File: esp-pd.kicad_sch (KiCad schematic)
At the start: 83 parts, among them J1 USB C Power, J2 USB C Data, J3 Power Out, J4 ESP PD Board pins, Q1 IRF7416, Q2 MMBT3904, SW1 Boot, SW2 Reset, SW3 Up, SW4 Down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

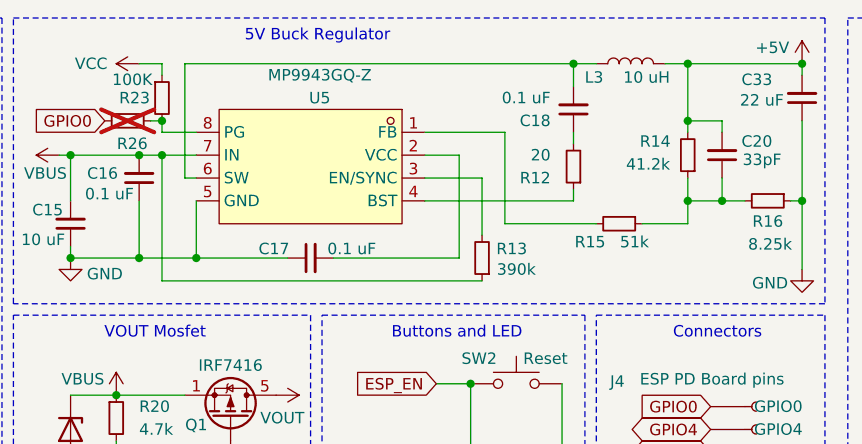
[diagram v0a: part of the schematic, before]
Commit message: added BST diode
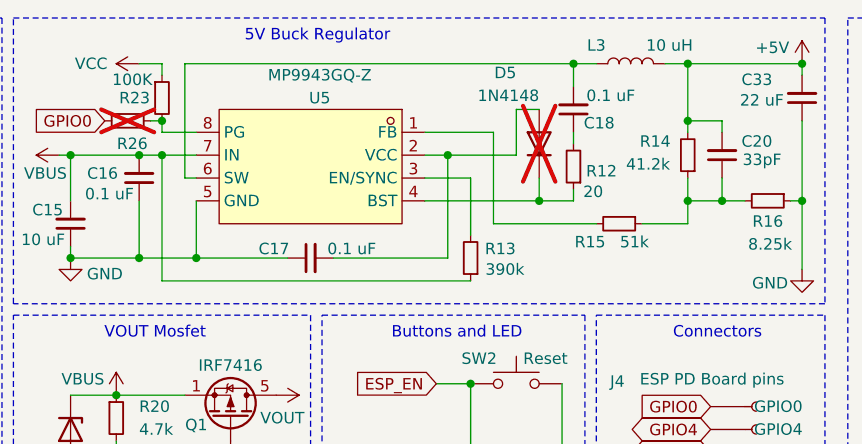
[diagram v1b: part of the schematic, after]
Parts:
- added D5: 1N4148, Diode_SMD:D_SOD-523, symbol Diode:1N4148WT
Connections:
- net at C17.2, U5.2 (VCC): now also D5.2 (A)
- net at R12.1, U5.4 (BST): now also D5.1 (K)
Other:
- moved on the sheet: R13
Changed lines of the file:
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@@
 	)
 	(junction
+		(at 149.86 31.75)
+		(diameter 0)
+		(color 0 0 0 0)
+	)
+	(junction
 		(at 57.15 95.25)
 		(diameter 0)
@@
 	)
 	(junction
+		(at 160.02 36.83)
+		(diameter 0)
+		(color 0 0 0 0)
+	)
+	(junction
 		(at 214.63 58.42)
 		(diameter 0)
@@
 	(wire
 		(pts
-			(xy 118.11 45.72) (xy 153.67 45.72)
+			(xy 118.11 45.72) (xy 152.4 45.72)
 		)
 		(stroke
@@
 	(wire
 		(pts
-			(xy 156.21 29.21) (xy 156.21 39.37)
+			(xy 154.94 29.21) (xy 154.94 39.37)
 		)
 		(stroke
@@
 	(wire
 		(pts
-			(xy 147.32 34.29) (xy 153.67 34.29)
+			(xy 147.32 34.29) (xy 152.4 34.29)
 		)
 		(stroke
@@
 	(wire
 		(pts
-			(xy 147.32 29.21) (xy 156.21 29.21)
+			(xy 147.32 29.21) (xy 154.94 29.21)
+		)
+		(stroke
+			(width 0)
+			(type default)
+		)
+	)
+	(wire
+		(pts
+			(xy 160.02 36.83) (xy 147.32 36.83)
 		)
 		(stroke
@@
 	(wire
 		(pts
-			(xy 151.13 43.18) (xy 151.13 31.75)
+			(xy 149.86 43.18) (xy 149.86 31.75)
 		)
 		(stroke
@@
 	(wire
 		(pts
-			(xy 156.21 39.37) (xy 166.37 39.37)
+			(xy 154.94 39.37) (xy 166.37 39.37)
 		)
 		(stroke
@@
 	(wire
 		(pts
-			(xy 137.16 43.18) (xy 151.13 43.18)
+			(xy 137.16 43.18) (xy 149.86 43.18)
 		)
 		(stroke
@@
 	(wire
 		(pts
-			(xy 151.13 31.75) (xy 147.32 31.75)
+			(xy 149.86 31.75) (xy 147.32 31.75)
 		)
 		(stroke
@@
 	(wire
 		(pts
-			(xy 153.67 34.29) (xy 153.67 40.64)
+			(xy 152.4 34.29) (xy 152.4 40.64)
 		)
 		(stroke
@@
 	(wire
 		(pts
+			(xy 160.02 26.67) (xy 157.48 26.67)
+		)
+		(stroke
+			(width 0)
+			(type default)
+		)
+	)
+	(wire
+		(pts
 			(xy 118.11 88.9) (xy 125.73 88.9)
 		)
@@
 	(wire
 		(pts
-			(xy 163.83 36.83) (xy 147.32 36.83)
+			(xy 163.83 36.83) (xy 160.02 36.83)
+		)
+		(stroke
+			(width 0)
+			(type default)
+		)
+	)
+	(wire
+		(pts
+			(xy 160.02 34.29) (xy 160.02 36.83)
 		)
 		(stroke
@@
 	(wire
 		(pts
+			(xy 157.48 31.75) (xy 149.86 31.75)
+		)
+		(stroke
+			(width 0)
+			(type default)
+		)
+	)
+	(wire
+		(pts
 			(xy 207.01 99.06) (xy 213.36 99.06)
 		)
@@
 	(wire
 		(pts
+			(xy 157.48 26.67) (xy 157.48 31.75)
+		)
+		(stroke
+			(width 0)
+			(type default)
+		)
+	)
+	(wire
+		(pts
 			(xy 121.92 29.21) (xy 118.11 29.21)
 		)
@@
 		(dnp no)
 		(property "Reference" "L3"
-			(at 166.116 23.114 90)
+			(at 166.37 19.558 90)
 			(effects
 				(font
@@
 		)
 		(property "Value" "10 uH"
-			(at 171.958 23.114 90)
+			(at 174.498 19.558 90)
 			(effects
 				(font
@@
 		(on_board yes)
 		(dnp no)
-		(fields_autoplaced yes)
 		(property "Reference" "C18"
-			(at 161.29 27.9338 0)
+			(at 168.402 28.194 0)
 			(effects
 				(font
@@
 		)
 		(property "Value" "0.1 uF"
-			(at 161.29 25.3938 0)
+			(at 170.688 25.146 0)
 			(effects
 				(font
@@
 	)
 	(symbol
+		(lib_id "Diode:1N4148WT")
+		(at 160.02 30.48 90)
+		(unit 1)
+		(exclude_from_sim no)
+		(in_bom yes)
+		(on_board yes)
+		(dnp yes)
+		(property "Reference" "D5"
+			(at 157.48 22.606 90)
+			(effects
+				(font
+					(size 1.27 1.27)
+				)
+				(justify left)
+			)
+		)
+		(property "Value" "1N4148"
+			(at 160.02 25.146 90)
+			(effects
+				(font
+					(size 1.27 1.27)
+				)
+				(justify left)
+			)
+		)
+		(property "Footprint" "Diode_SMD:D_SOD-523"
+			(at 164.465 30.48 0)
+			(effects
+				(font
+					(size 1.27 1.27)
+				)
+				(hide yes)
+			)
+		)
+		(property "Datasheet" "https://www.diodes.com/assets/Datasheets/ds30396.pdf"
+			(at 160.02 30.48 0)
+			(effects
+				(font
+					(size 1.27 1.27)
+				)
+				(hide yes)
+			)
+		)
+		(property "Description" "75V 0.15A Fast switching Diode, SOD-523"
+			(at 160.02 30.48 0)
+			(effects
+				(font
+					(size 1.27 1.27)
+				)
+				(hide yes)
+			)
+		)
+		(property "Sim.Device" "D"
+			(at 160.02 30.48 0)
+			(effects
+				(font
+					(size 1.27 1.27)
+				)
+				(hide yes)
+			)
+		)
+		(property "Sim.Pins" "1=K 2=A"
+			(at 160.02 30.48 0)
+			(effects
+				(font
+					(size 1.27 1.27)
+				)
+				(hide yes)
+			)
+		)
+		(pin "2"
+		)
+		(pin "1"
+		)
+		(instances
+			(project "esp-pd"
+				(path "/19120343-bffe-46ad-ae62-c8e5f852fdaa"
+					(reference "D5")
+					(unit 1)
+				)
+			)
+		)
+	)
+	(symbol
 		(lib_id "Device:C_Small")
 		(at 199.39 48.26 180)
@@
 		(on_board yes)
 		(dnp no)
-		(fields_autoplaced yes)
 		(property "Reference" "R12"
-			(at 161.29 34.2901 0)
+			(at 168.656 33.528 0)
 			(effects
 				(font
@@
 		)
 		(property "Value" "20"
-			(at 161.29 31.7501 0)
+			(at 167.132 35.814 0)
 			(effects
 				(font
@@
 	(symbol
 		(lib_id "Device:R_Small")
-		(at 153.67 43.18 180)
+		(at 152.4 43.18 180)
 		(unit 1)
 		(exclude_from_sim no)
@@
 		(dnp no)
 		(property "Reference" "R13"
-			(at 156.972 42.164 0)
+			(at 155.702 42.164 0)
 			(effects
 				(font
@@
 		)
 		(property "Value" "390k"
-			(at 157.48 44.45 0)
+			(at 156.21 44.45 0)
 			(effects
 				(font
@@
 		)
 		(property "Footprint" "Resistor_SMD:R_0402_1005Metric"
-			(at 153.67 43.18 0)
+			(at 152.4 43.18 0)
 			(effects
 				(font
@@
 		)
 		(property "Datasheet" "~"
-			(at 153.67 43.18 0)
+			(at 152.4 43.18 0)
 			(effects
 				(font
@@
 		)
 		(property "Description" "Resistor, small symbol"
-			(at 153.67 43.18 0)
+			(at 152.4 43.18 0)
 			(effects
 				(font

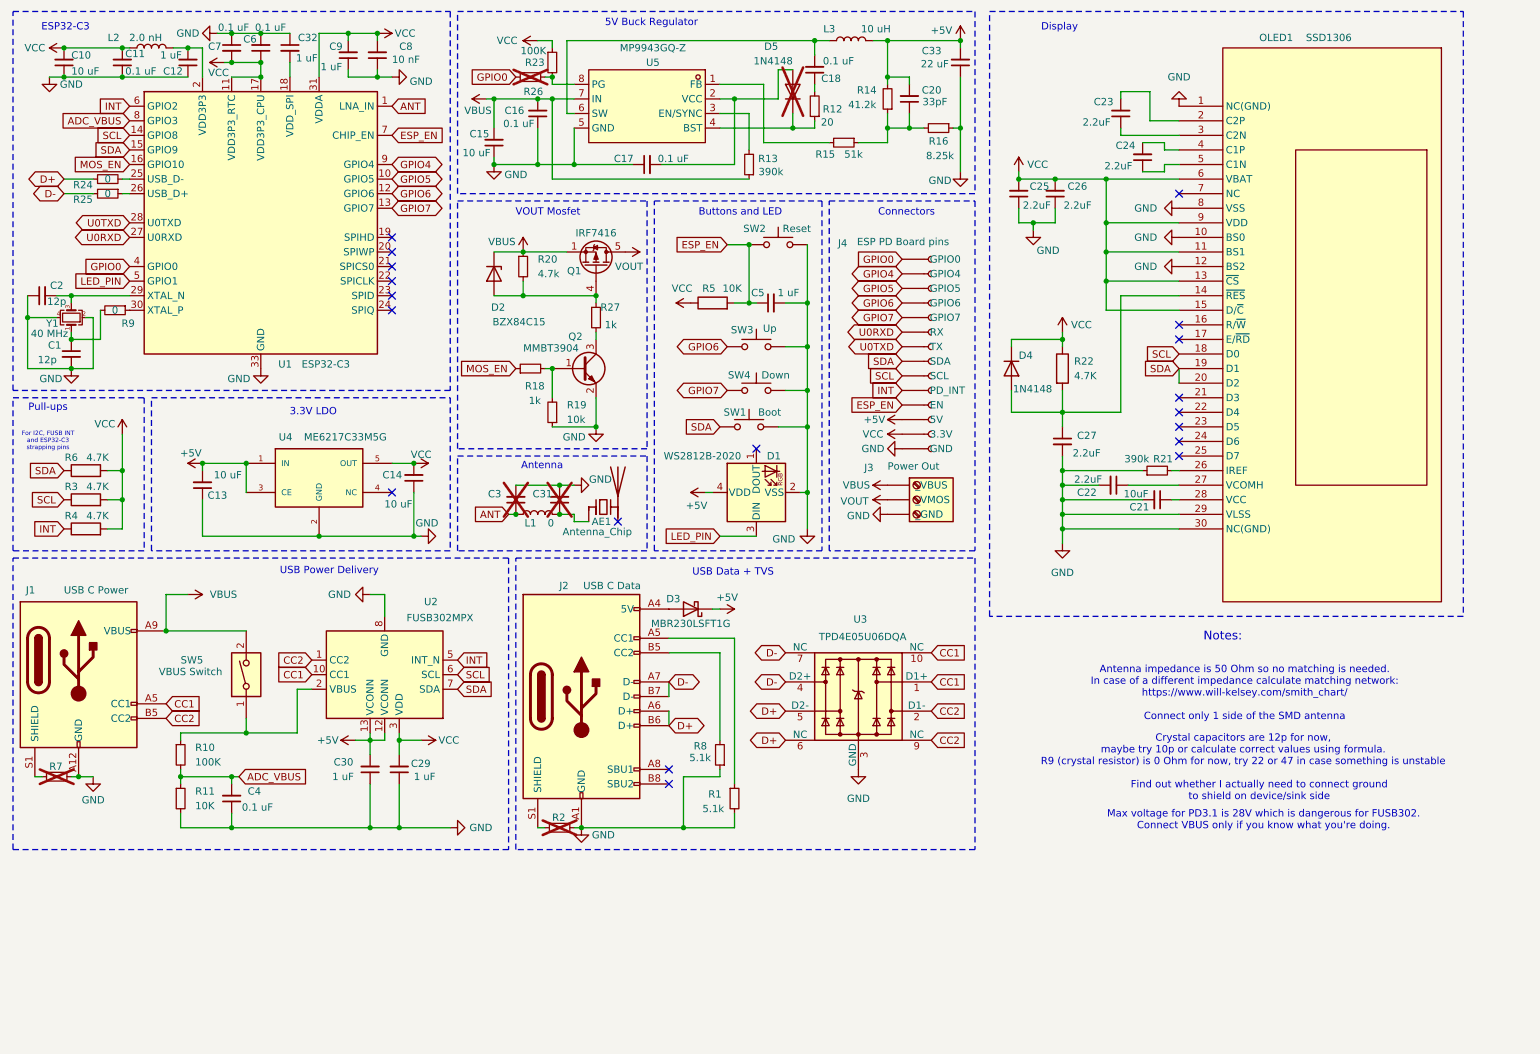
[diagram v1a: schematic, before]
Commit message: added INA226
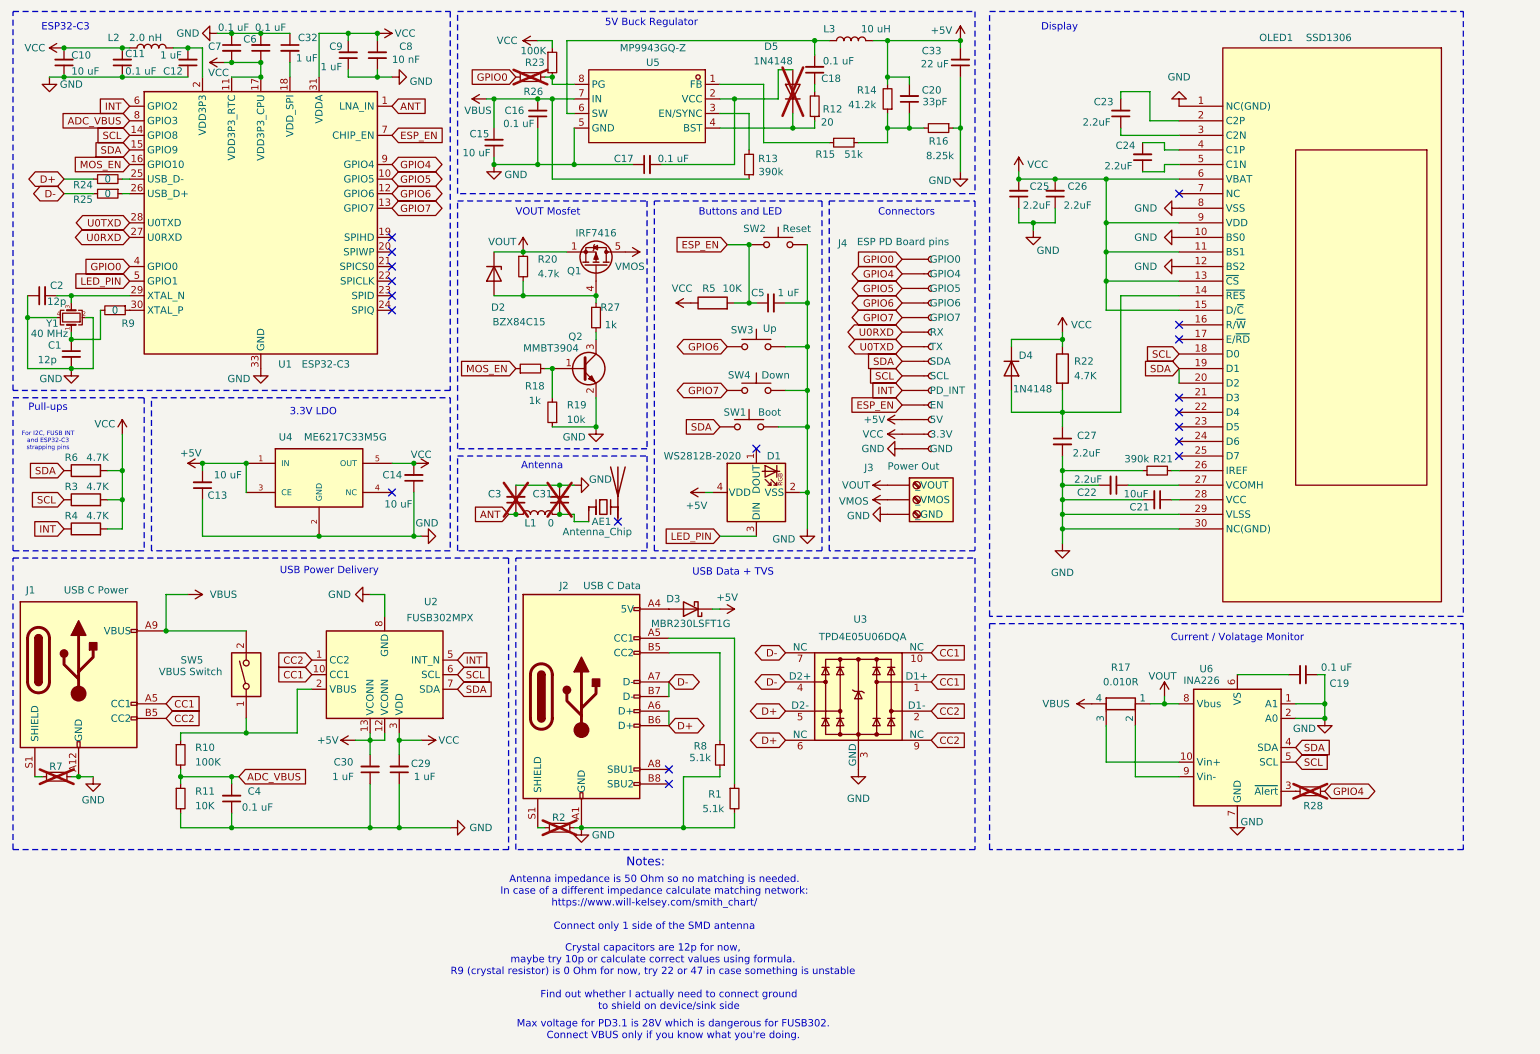
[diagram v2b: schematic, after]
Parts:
- added C19: 0.1 uF, Capacitor_SMD:C_0402_1005Metric, symbol Device:C_Small
- added R17: 0.010R, pb_board:R_Shunt_Vishay_WSK2512_6332Metric_new, symbol Device:R_Shunt
- added R28: 0, Resistor_SMD:R_0402_1005Metric, symbol Device:R_Small
- added U6: INA226, Package_SO:VSSOP-10_3x3mm_P0.5mm, symbol Sensor_Energy:INA226
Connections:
- net GND: now also C19.1, U6.1 (A1), U6.2 (A0), U6.7 (GND)
- net GPIO4: now also R28.1
- net SCL: now also U6.5 (SCL)
- net SDA: now also U6.4 (SDA)
- net VBUS: now also R17.4; no longer D2.3 (K), J3.1 (_VBUS), Q1.1 (S), Q1.2 (S), Q1.3 (S), R20.1
- net VOUT: now also D2.3 (K), J3.1 (_VOUT), Q1.1 (S), Q1.2 (S), Q1.3 (S), R20.1, R17.1, U6.8 (Vbus); no longer J3.2 (_VMOS), Q1.5 (D), Q1.6 (D), Q1.7 (D), Q1.8 (D)
- new net: R17.3, U6.10 (Vin+)
- new net: R28.2, U6.3 (~{Alert})
- new net: C19.2, U6.6 (VS)
- new net: R17.2, U6.9 (Vin-)
- new net VMOS: J3.2 (_VMOS), Q1.5 (D), Q1.6 (D), Q1.7 (D), Q1.8 (D)
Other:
- note added: "Current / Volatage Monitor"
